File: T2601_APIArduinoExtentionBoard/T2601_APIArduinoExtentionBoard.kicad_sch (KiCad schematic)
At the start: 75 parts, among them J1 Conn_01x10_Socket, J11 Conn_01x04_Pin, J12 Screw_Terminal_01x02, J13 Conn_01x04_Pin, J14 Screw_Terminal_01x02, J15 Conn_02x08_Counter_Clockwise, J2 Conn_01x10_Socket, J3 Conn_01x10_Socket, J4 Conn_01x10_Socket, J5 Screw_Terminal_01x08, J6 Screw_Terminal_01x08, J7 Conn_02x03_Counter_Clockwise, J8 Conn_01x04, J9 Conn_02x08_Counter_Clockwise, U1 ATMEGA328P-AU, X1 X322516MOB4SI

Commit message: V0.5 - Mounting Hole + Silkscreen
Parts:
- added C4: 100nF, PCM_JLCPCB:C_0402, symbol PCM_JLCPCB-Capacitors:0402,100nF
- added JP1, JP2, JP3, JP4, JP5, JP6: SolderJumper_2_Open, Jumper:SolderJumper-2_P1.3mm_Open_RoundedPad1.0x1.5mm, symbol Jumper:SolderJumper_2_Open
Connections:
- net GND: now also C4.2, JP1.1 (A), JP2.1 (A), JP3.1 (A), JP4.1 (A), JP5.1 (A), JP6.1 (A)
- net GNDPWR: now also JP1.2 (B), JP2.2 (B), JP3.2 (B), JP4.2 (B), JP5.2 (B), JP6.2 (B)
- net RX: now also J15.7 (Pin_7); no longer J9.10 (Pin_10)
- net TX: now also J9.10 (Pin_10); no longer J15.7 (Pin_7)
- net at U1.20 (AREF): now also C4.1

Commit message: Silkescreen Mod
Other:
- note added: "License Copyright (C) 2026 HackHype This project is licensed under CERN OHL-S v2. See the LICENSE file for details. ```"
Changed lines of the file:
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@@
+		)
+	)
+	(text "License\nCopyright (C) 2026 HackHype\nThis project is licensed under CERN OHL-S v2.\nSee the LICENSE file for details.\n```\n"
+		(exclude_from_sim no)
+		(at 14.478 192.278 0)
+		(effects
+			(font
+				(size 1.27 1.27)
+			)
+			(justify left)
 		)
 	)

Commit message: Silkscreen/Logo/ComPin Attribution
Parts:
- added JP10, JP11, JP12, JP7, JP8, JP9: SolderJumper_2_Open, Jumper:SolderJumper-2_P1.3mm_Open_RoundedPad1.0x1.5mm, symbol Jumper:SolderJumper_2_Open
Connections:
- net GEN_RESET: now also J15.13 (Pin_13), J9.13 (Pin_13); no longer J15.11 (Pin_11), J9.12 (Pin_12)
- net GND: now also J15.5 (Pin_5), J15.7 (Pin_7), J15.8 (Pin_8), J9.10 (Pin_10), J9.12 (Pin_12), J9.14 (Pin_14), J9.6 (Pin_6), J9.8 (Pin_8), JP10.1 (A), JP11.1 (A), JP12.1 (A), JP7.1 (A), JP8.1 (A), JP9.1 (A); no longer J15.15 (Pin_15), J15.16 (Pin_16), J9.11 (Pin_11), J9.13 (Pin_13), J9.15 (Pin_15), J9.16 (Pin_16)
- net GNDPWR: now also JP10.2 (B), JP11.2 (B), JP12.2 (B), JP7.2 (B), JP8.2 (B), JP9.2 (B)
- net RX: now also J9.11 (Pin_11); no longer J15.7 (Pin_7)
- net TX: now also J15.11 (Pin_11); no longer J9.10 (Pin_10)
- net UART_BACK: now also J15.9 (Pin_9), J9.9 (Pin_9); no longer J15.5 (Pin_5), J9.6 (Pin_6)
- no-connect marks 5 -> 6
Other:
- note added: "License Copyright (C) 2026 HackHype This project is licensed under CERN OHL-S v2. See the LICENSE file for details."
- note removed: "License Copyright (C) 2026 HackHype This project is licensed under CERN OHL-S v2. See the LICENSE file for details. ```"
- moved on the sheet: C1, C2, C3, C4, J1, J11, J12, J13, J14, J15, J2, J3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

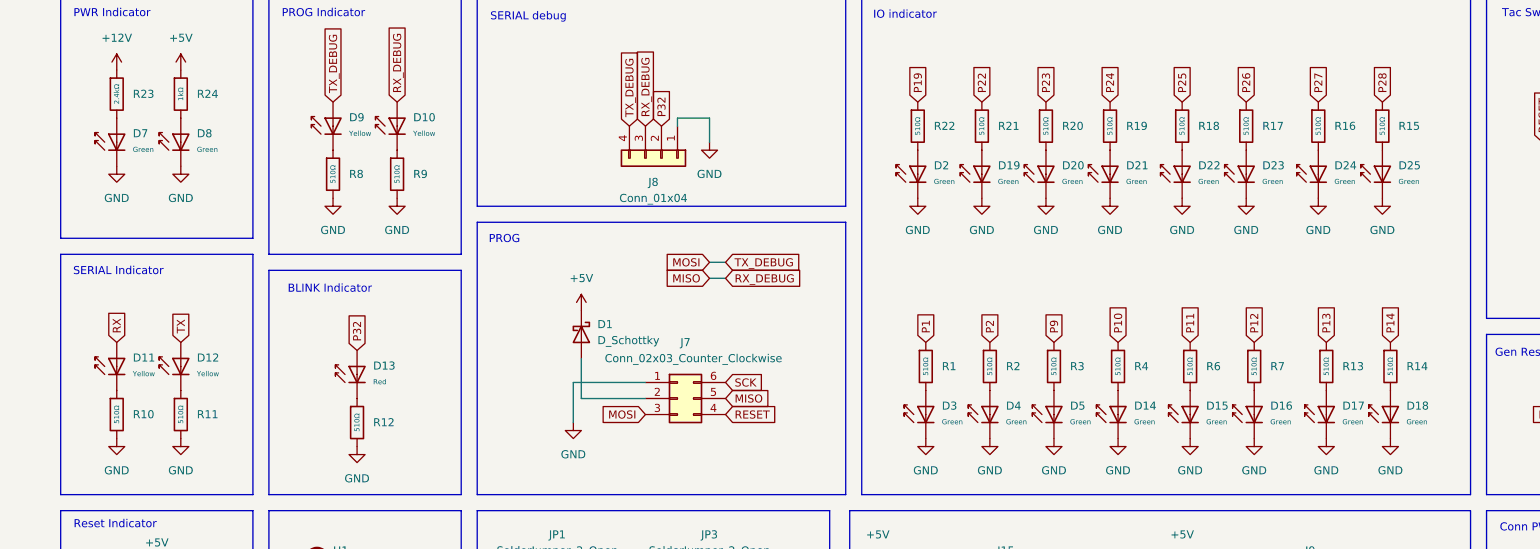
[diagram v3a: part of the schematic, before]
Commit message: Side Tolerances + Resistor Value
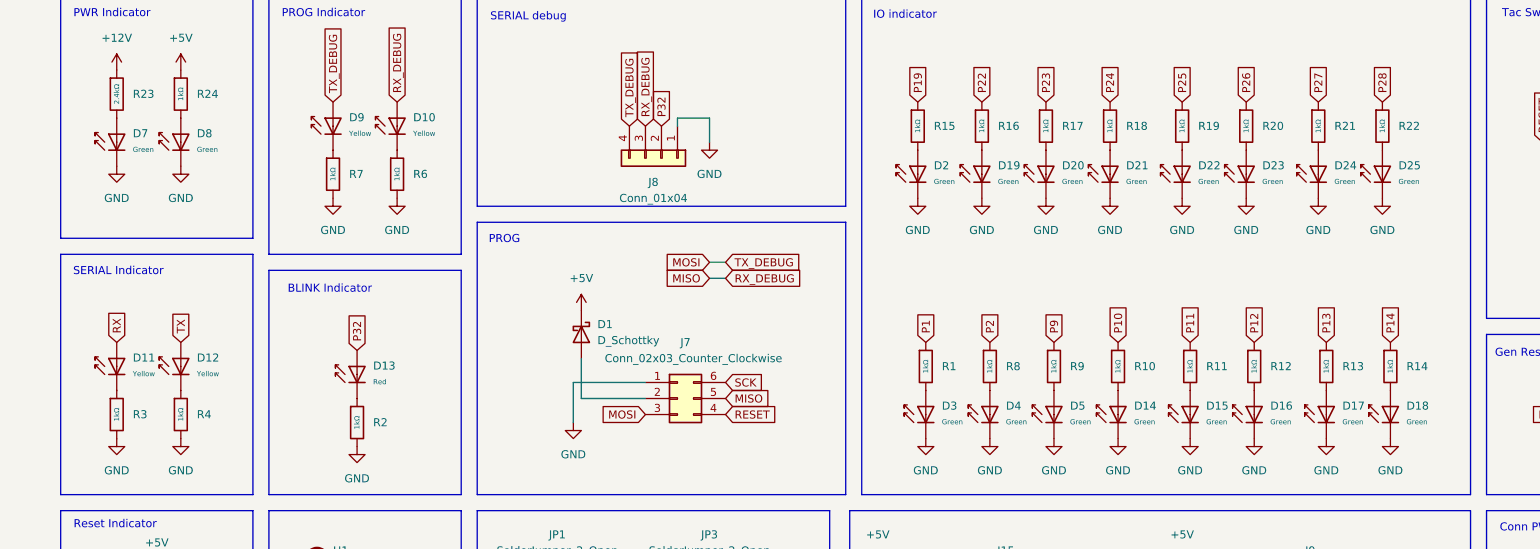
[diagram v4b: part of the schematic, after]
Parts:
- removed R1, R10, R11, R12, R13, R14, R15, R16, R17, R18, R19, R2, R20, R21, R22, R3, R4, R6, R7, R8, R9: 510Ω, PCM_JLCPCB:R_0402, symbol PCM_JLCPCB-Resistors:0402,510Ω
- removed R25: 1kΩ, PCM_JLCPCB:R_0603, symbol PCM_JLCPCB-Resistors:0603,1kΩ
- added R1, R10, R11, R12, R13, R14, R15, R16, R17, R18, R19, R2, R20, R21, R22, R25, R3, R4, R6, R7, R8, R9: 1kΩ, PCM_JLCPCB:R_0402, symbol PCM_JLCPCB-Resistors:0402,1kΩ
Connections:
- net +5V: now also R25.1
- net GND: now also R2.2, R3.2, R4.2, R6.2, R7.2
- net P1: now also R1.1
- net P10: now also R10.1
- net P11: now also R11.1
- net P12: now also R12.1
- net P13: now also R13.1
- net P14: now also R14.1
- net P19: now also R15.1
- net P2: now also R8.1
- net P22: now also R16.1
- net P23: now also R17.1
- net P24: now also R18.1
- net P25: now also R19.1
- net P26: now also R20.1
- net P27: now also R21.1
- net P28: now also R22.1
- net P9: now also R9.1
- net at D5.2: now also R9.2
- net at D13.1: now also R2.1
- net at D20.2: now also R17.2
- net at D4.2: now also R8.2
- net at D12.1: now also R4.1
- net at D15.2: now also R11.2
- net at D11.1: now also R3.1
- net at D23.2: now also R20.2
- net at D2.2: now also R15.2
- net at D26.2: now also R25.2
- net at D10.1: now also R6.1
- net at D18.2: now also R14.2
- net at D21.2: now also R18.2
- net at D16.2: now also R12.2
- net at D19.2: now also R16.2
- net at D14.2: now also R10.2
- net at D22.2: now also R19.2
- net at D3.2: now also R1.2
- net at D9.1: now also R7.1
- net at D25.2: now also R22.2
- net at D24.2: now also R21.2
- net at D17.2: now also R13.2

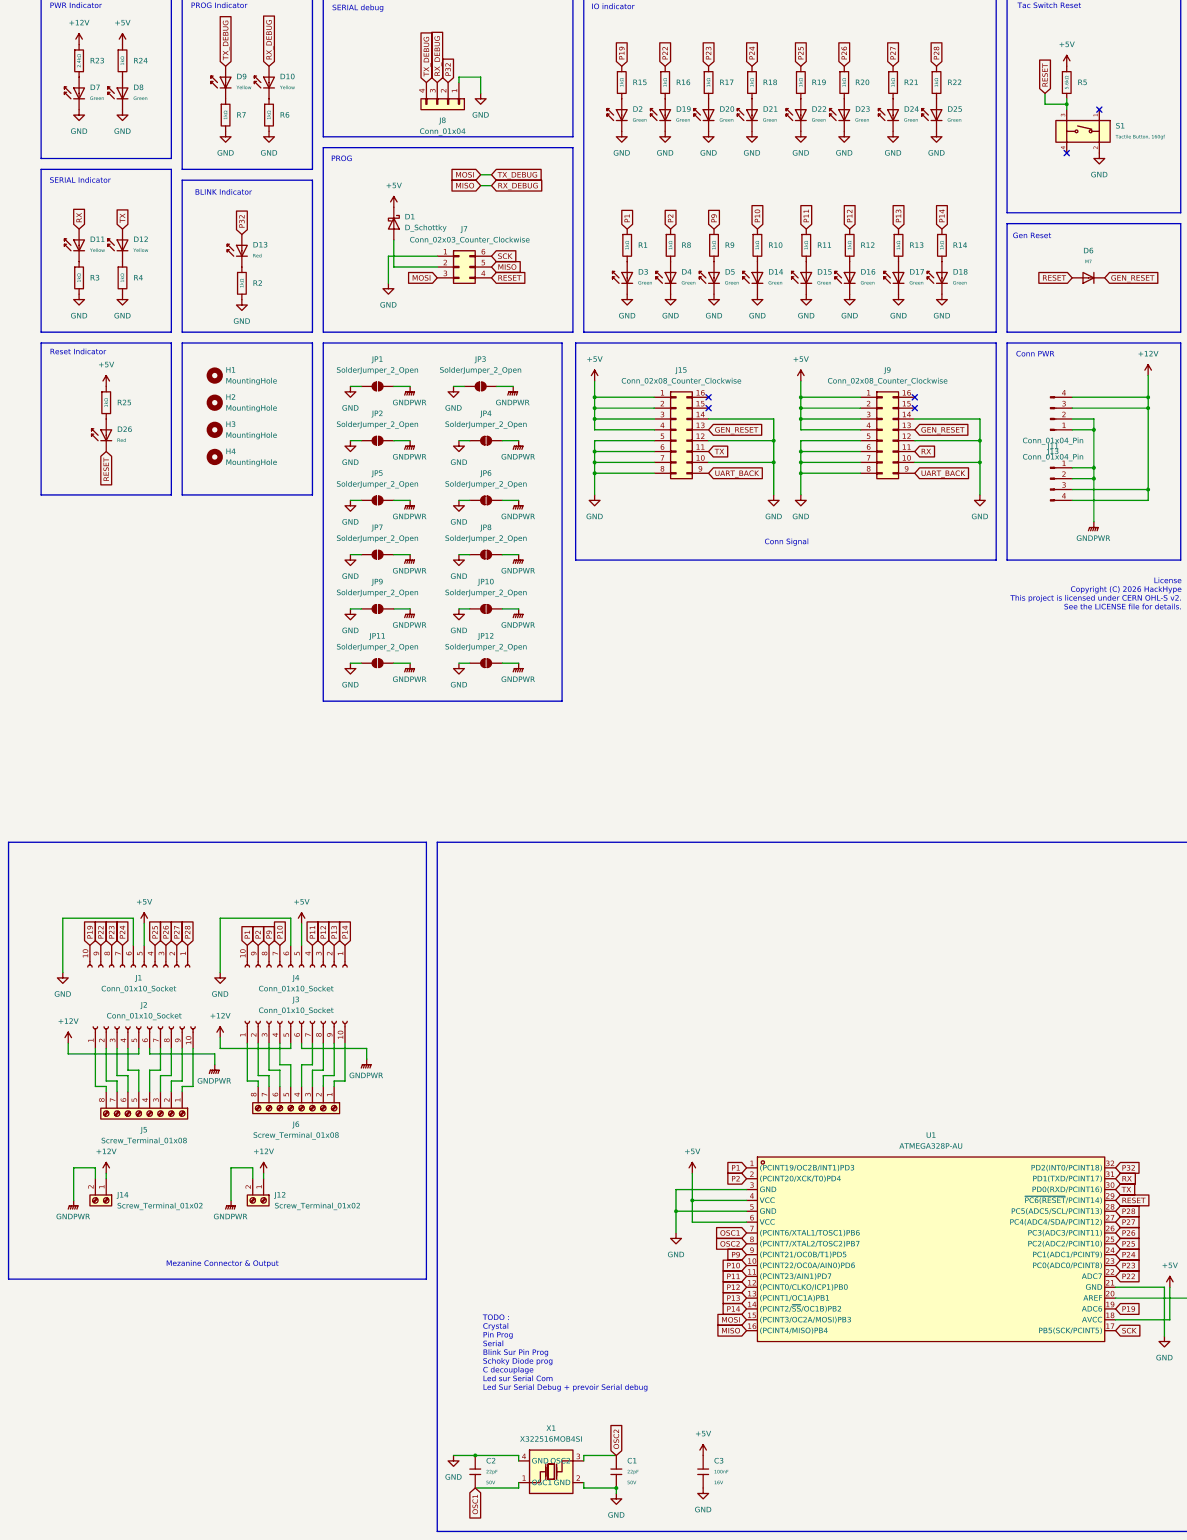
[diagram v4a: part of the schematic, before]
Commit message: Capacitor + plane correction
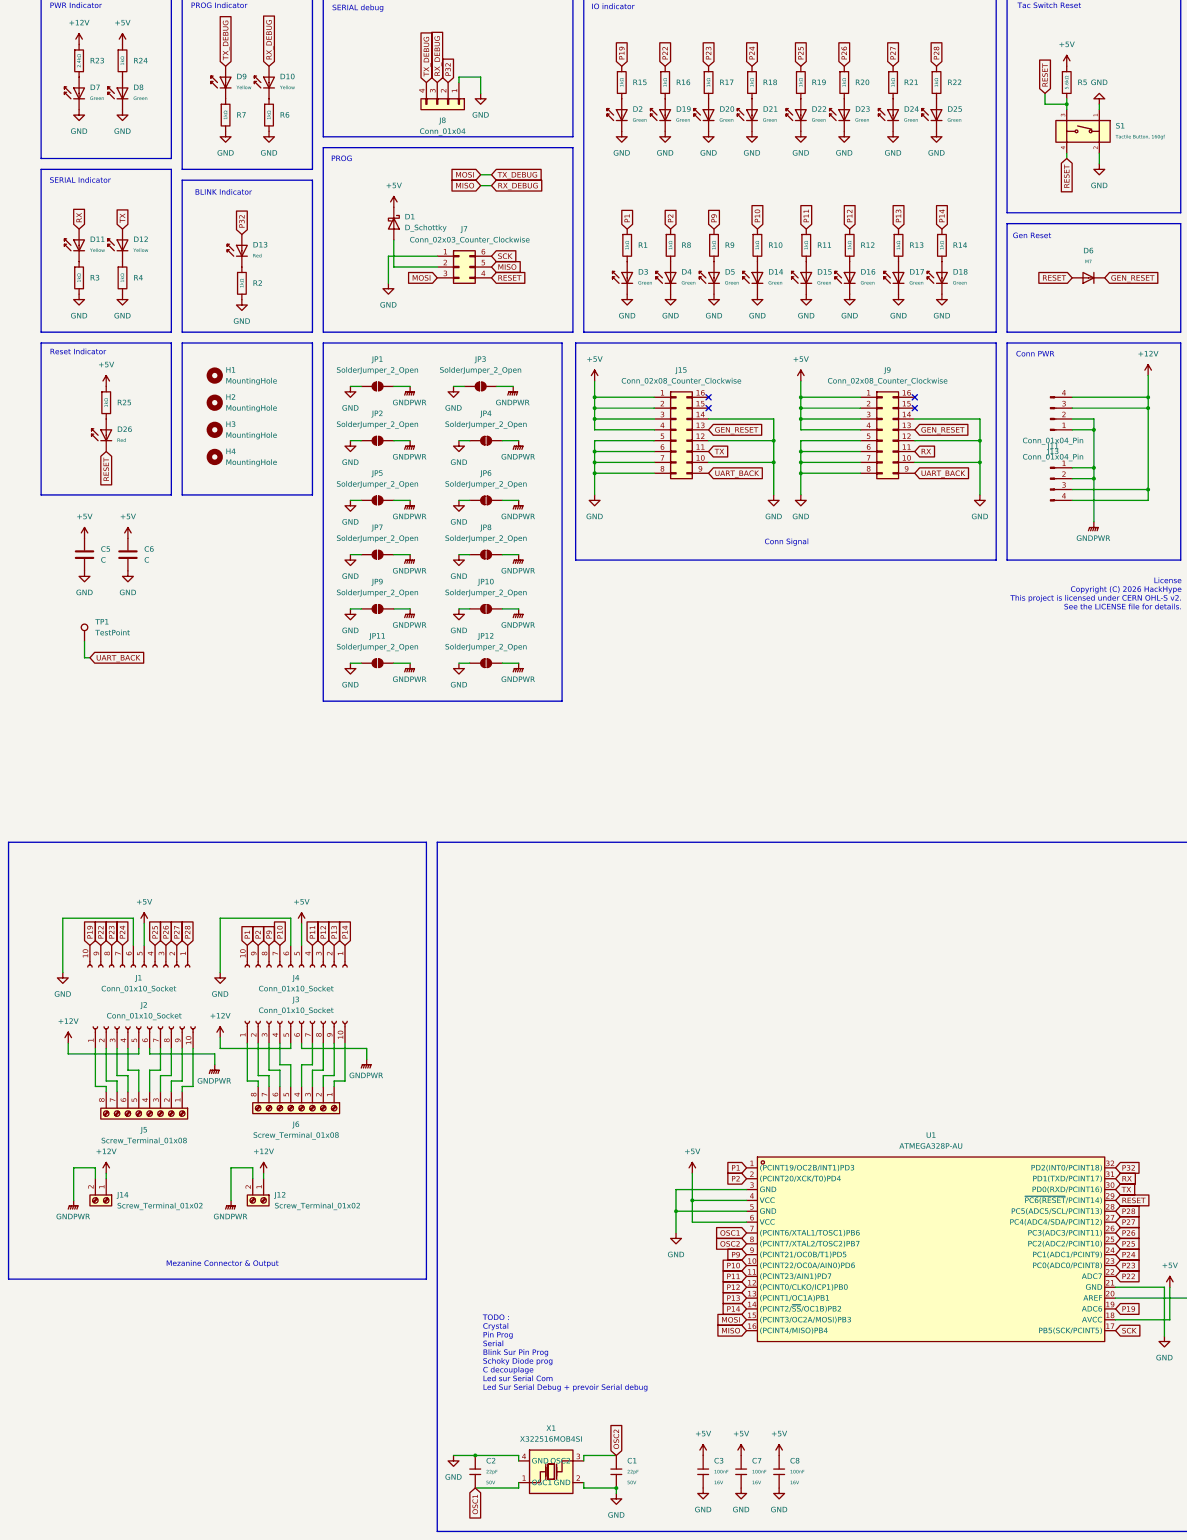
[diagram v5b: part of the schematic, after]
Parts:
- added C5, C6: C, Capacitor_THT:C_Radial_D6.3mm_H11.0mm_P2.50mm, symbol Device:C
- added C7, C8: 100nF, PCM_JLCPCB:C_0402, symbol PCM_JLCPCB-Capacitors:0402,100nF
- added TP1: TestPoint, TestPoint:TestPoint_Pad_D2.0mm, symbol Connector:TestPoint
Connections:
- net +5V: now also C5.1, C6.1, C7.1, C8.1
- net GND: now also S1.1 (A), C5.2, C6.2, C7.2, C8.2
- net RESET: now also S1.4 (D)
- net UART_BACK: now also TP1.1
- no-connect marks 6 -> 4
